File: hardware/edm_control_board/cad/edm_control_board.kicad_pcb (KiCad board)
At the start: 4 copper layers, 240 x 100 mm, 63 parts, among them J401 Conn_02x08_Odd_Even, J402 Conn_01x02, J403 Conn_01x02, J404 Conn_01x02, J405 Conn_01x06, Q201 BSS214NW, Q202 BSS214NW, Q203 BSS214NW, Q204 BSS214NW, SW501 SW_Push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

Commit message: Routing
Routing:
- net /Controller/LCD_DB6: track 75.6 -> 78.1 mm
- net /Controller/LCD_DB5: track 75.3 -> 76.8 mm
- net /Controller/LCD_DB7: track 77.8 -> 79.3 mm
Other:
- board text added: "EDM Control Board 2018-02-18 JS"
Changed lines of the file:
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@@
   (general
     (thickness 1.6)
-    (drawings 34)
-    (tracks 496)
+    (drawings 35)
+    (tracks 500)
     (zones 0)
     (modules 63)
@@
   )
   (setup
-    (last_trace_width 1)
+    (last_trace_width 0.25)
     (user_trace_width 0.25)
     (user_trace_width 0.5)
@@
     )
   )
+  (gr_text "EDM Control Board 2018-02-18 JS" (at 16 -3) (layer B.SilkS)
+    (effects (font (size 1.5 1.5) (thickness 0.3)) (justify right mirror))
+  )
   (gr_text SWDIO (at 129.74 -93.33 270) (layer B.SilkS)
     (effects (font (size 1 1) (thickness 0.2)) (justify left mirror))
@@
   (segment (start 171.25 -65.532055) (end 152.782055 -84) (width 0.25) (layer B.Cu) (net 39))
   (segment (start 171.25 -63.95) (end 171.25 -65.532055) (width 0.25) (layer B.Cu) (net 39))
-  (segment (start 152.6456 -83.500044) (end 107.040044 -83.500044) (width 0.25) (layer B.Cu) (net 40))
-  (segment (start 170.75 -65.395644) (end 152.6456 -83.500044) (width 0.25) (layer B.Cu) (net 40))
-  (segment (start 105.749999 -82.209999) (end 105 -81.46) (width 0.25) (layer B.Cu) (net 40))
+  (segment (start 105.04 -81.5) (end 105 -81.46) (width 0.25) (layer B.Cu) (net 40))
   (segment (start 170.75 -63.95) (end 170.75 -65.395644) (width 0.25) (layer B.Cu) (net 40))
-  (segment (start 107.040044 -83.500044) (end 105.749999 -82.209999) (width 0.25) (layer B.Cu) (net 40))
-  (segment (start 105 -78.92) (end 109.130033 -83.050033) (width 0.25) (layer B.Cu) (net 41))
-  (segment (start 169.25 -64.7) (end 169.25 -63.95) (width 0.25) (layer B.Cu) (net 41))
-  (segment (start 169.25 -66.259233) (end 169.25 -64.7) (width 0.25) (layer B.Cu) (net 41))
+  (segment (start 108.200044 -83.500044) (end 106.2 -81.5) (width 0.25) (layer B.Cu) (net 40))
+  (segment (start 152.6456 -83.500044) (end 108.200044 -83.500044) (width 0.25) (layer B.Cu) (net 40))
+  (segment (start 170.75 -65.395644) (end 152.6456 -83.500044) (width 0.25) (layer B.Cu) (net 40))
+  (segment (start 106.2 -81.5) (end 105.04 -81.5) (width 0.25) (layer B.Cu) (net 40))
+  (segment (start 106.5 -81.109233) (end 108.4408 -83.050033) (width 0.25) (layer B.Cu) (net 41))
+  (segment (start 105 -78.92) (end 106.5 -80.42) (width 0.25) (layer B.Cu) (net 41))
+  (segment (start 106.5 -80.42) (end 106.5 -81.109233) (width 0.25) (layer B.Cu) (net 41))
+  (segment (start 108.4408 -83.050033) (end 152.4592 -83.050033) (width 0.25) (layer B.Cu) (net 41))
   (segment (start 152.4592 -83.050033) (end 169.25 -66.259233) (width 0.25) (layer B.Cu) (net 41))
-  (segment (start 109.130033 -83.050033) (end 152.4592 -83.050033) (width 0.25) (layer B.Cu) (net 41))
-  (segment (start 105 -76.38) (end 111.220022 -82.600022) (width 0.25) (layer B.Cu) (net 42))
+  (segment (start 169.25 -66.259233) (end 169.25 -64.7) (width 0.25) (layer B.Cu) (net 41))
+  (segment (start 169.25 -64.7) (end 169.25 -63.95) (width 0.25) (layer B.Cu) (net 41))
   (segment (start 168.75 -64.7) (end 168.75 -63.95) (width 0.25) (layer B.Cu) (net 42))
-  (segment (start 111.220022 -82.600022) (end 152.2728 -82.600022) (width 0.25) (layer B.Cu) (net 42))
-  (segment (start 152.2728 -82.600022) (end 168.75 -66.122822) (width 0.25) (layer B.Cu) (net 42))
   (segment (start 168.75 -66.122822) (end 168.75 -64.7) (width 0.25) (layer B.Cu) (net 42))
-  (segment (start 105 -73.84) (end 105.749999 -74.589999) (width 0.25) (layer B.Cu) (net 43))
-  (segment (start 105.749999 -74.589999) (end 105.749999 -74.84077) (width 0.25) (layer B.Cu) (net 43))
+  (segment (start 152.2728 -82.600022) (end 168.75 -66.122822) (width 0.25) (layer B.Cu) (net 42))
+  (segment (start 108.6272 -82.600022) (end 152.2728 -82.600022) (width 0.25) (layer B.Cu) (net 42))
+  (segment (start 105 -76.38) (end 106.950011 -78.330011) (width 0.25) (layer B.Cu) (net 42))
+  (segment (start 106.950011 -78.330011) (end 106.950011 -80.922833) (width 0.25) (layer B.Cu) (net 42))
+  (segment (start 106.950011 -80.922833) (end 108.6272 -82.600022) (width 0.25) (layer B.Cu) (net 42))
   (segment (start 168.25 -64.7) (end 168.25 -63.95) (width 0.25) (layer B.Cu) (net 43))
-  (segment (start 152.0864 -82.150011) (end 168.25 -65.986411) (width 0.25) (layer B.Cu) (net 43))
-  (segment (start 113.05924 -82.150011) (end 152.0864 -82.150011) (width 0.25) (layer B.Cu) (net 43))
-  (segment (start 105.749999 -74.84077) (end 113.05924 -82.150011) (width 0.25) (layer B.Cu) (net 43))
   (segment (start 168.25 -65.986411) (end 168.25 -64.7) (width 0.25) (layer B.Cu) (net 43))
-  (segment (start 109.5 -77.95436) (end 113.24564 -81.7) (width 0.25) (layer B.Cu) (net 44))
-  (segment (start 105 -71.3) (end 106.8 -71.3) (width 0.25) (layer B.Cu) (net 44))
-  (segment (start 106.8 -71.3) (end 109.5 -74) (width 0.25) (layer B.Cu) (net 44))
-  (segment (start 109.5 -74) (end 109.5 -77.95436) (width 0.25) (layer B.Cu) (net 44))
-  (segment (start 113.24564 -81.7) (end 151.9 -81.7) (width 0.25) (layer B.Cu) (net 44))
-  (segment (start 151.9 -81.7) (end 167.75 -65.85) (width 0.25) (layer B.Cu) (net 44))
+  (segment (start 152.0864 -82.150011) (end 168.25 -65.986411) (width 0.25) (layer B.Cu) (net 43))
+  (segment (start 108.8136 -82.150011) (end 152.0864 -82.150011) (width 0.25) (layer B.Cu) (net 43))
+  (segment (start 107.449989 -80.7864) (end 108.8136 -82.150011) (width 0.25) (layer B.Cu) (net 43))
+  (segment (start 105 -73.84) (end 107.449989 -76.289989) (width 0.25) (layer B.Cu) (net 43))
+  (segment (start 107.449989 -76.289989) (end 107.449989 -80.7864) (width 0.25) (layer B.Cu) (net 43))
   (segment (start 167.75 -65.85) (end 167.75 -63.95) (width 0.25) (layer B.Cu) (net 44))
+  (segment (start 151.9 -81.7) (end 167.75 -65.85) (width 0.25) (layer B.Cu) (net 44))
+  (segment (start 109 -81.7) (end 151.9 -81.7) (width 0.25) (layer B.Cu) (net 44))
+  (segment (start 107.9 -80.6) (end 109 -81.7) (width 0.25) (layer B.Cu) (net 44))
+  (segment (start 105 -71.3) (end 107.9 -74.2) (width 0.25) (layer B.Cu) (net 44))
+  (segment (start 107.9 -74.2) (end 107.9 -80.6) (width 0.25) (layer B.Cu) (net 44))
   (segment (start 168.25 -52.55) (end 168.25 -47.605) (width 0.25) (layer B.Cu) (net 45))
   (segment (start 168.25 -47.605) (end 168.555 -47.3) (width 0.25) (layer B.Cu) (net 45))

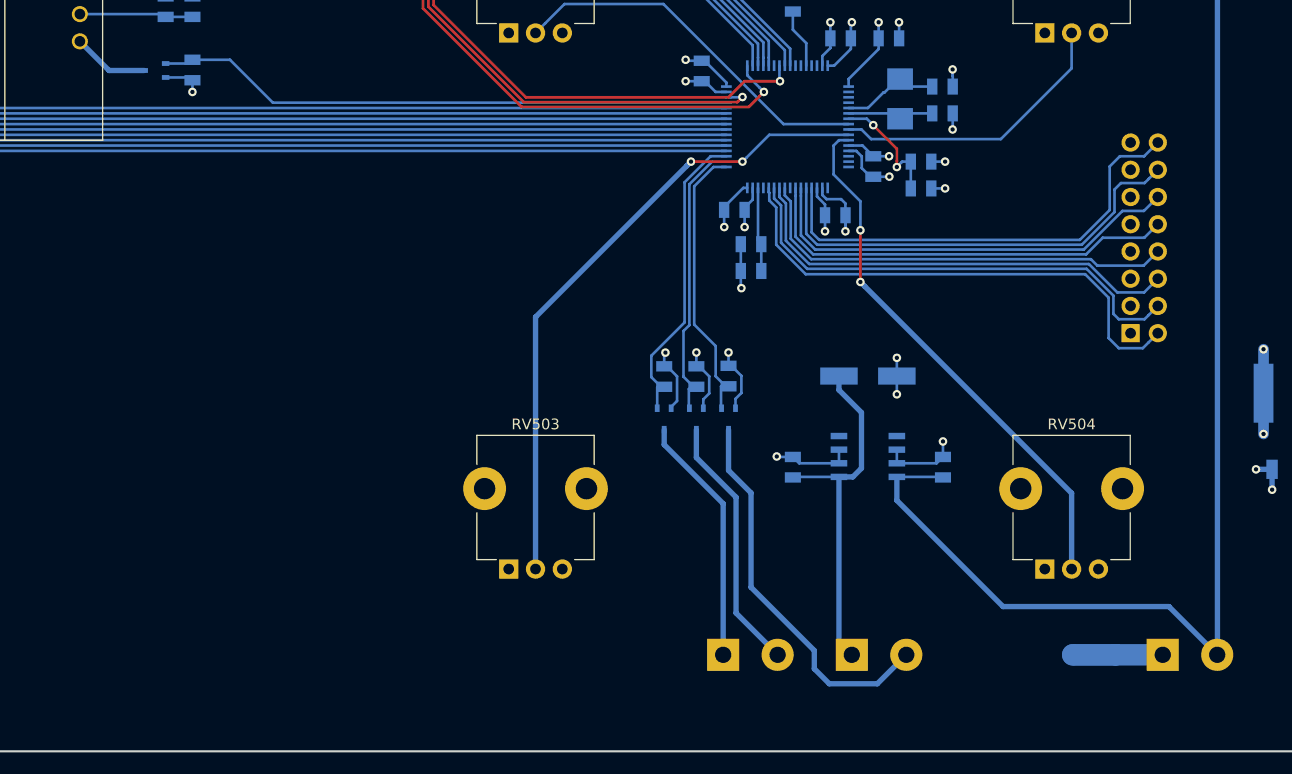
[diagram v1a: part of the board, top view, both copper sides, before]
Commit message: Add water pump to pcb
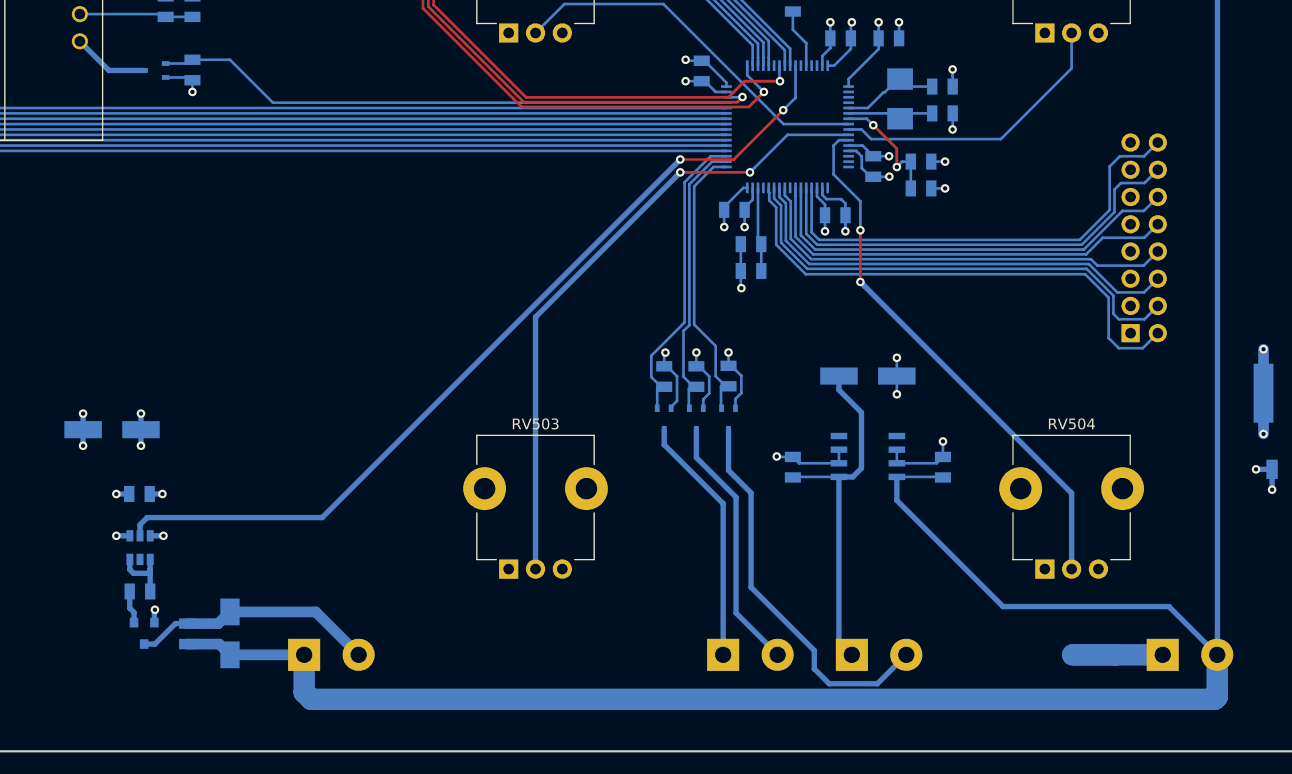
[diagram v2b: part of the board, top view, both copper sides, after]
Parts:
- added C601: 10u, Capacitor_SMD:CP_Elec_6.3x5.3, B.Cu at (108.0, -30.0)
- added C602: 100n, Capacitor_SMD:C_0805_2012Metric, B.Cu at (110.6, -24.0)
- added C603: 1n, Capacitor_SMD:C_0805_2012Metric, B.Cu at (115.0, -11.0)
- added D601: CDBA140-G, Diode_SMD:D_SMA, B.Cu at (119.0, -11.0)
- added J406: Conn_01x02, TerminalBlock:TerminalBlock_bornier-2_P5.08mm, B.Cu at (125.9, -9.00)
- added Q601: DMN3404L-7, Package_TO_SOT_SMD:SOT-23, B.Cu at (111.0, -11.0)
- added R601: 4R99, Resistor_SMD:R_0805_2012Metric, B.Cu at (110.6, -14.9)
- added U601: ZXGD3009E6, Package_TO_SOT_SMD:SOT-23-6, B.Cu at (110.6, -19.0)
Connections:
- U301 pad 58: Net-(U301-Pad58) -> /Controller/Water_Pump_PWM
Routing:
- net +24V: track 139.2 -> 243.4 mm
- net /Controller/Water_Pump_PWM: track 0.00 -> 81.7 mm, vias 0 -> 2
- net /Connectors/Water_Pump_NEG: track 0.00 -> 22.9 mm
- net GND: track 105.8 -> 112.5 mm, vias 29 -> 34
- net Net-(R601-Pad2): track 0.00 -> 6.39 mm
- net +3V3: track 42.8 -> 48.3 mm, vias 12 -> 16
- net Net-(Q601-Pad1): track 0.00 -> 3.07 mm
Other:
- board text added: "PUMP+"
- board text added: "PUMP-"

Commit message: Added copper planes to front and back. Added gerber files.
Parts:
- moved RV201 8.00 mm to (41.0, -85.0)
- moved J405 3.00 mm to (122.1, -88.1)
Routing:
- net /Controller/LCD_V0: track 21.8 -> 14.3 mm
- net +24V: track 243.4 -> 239.0 mm
- net /Controller/POT_4: track 50.3 -> 54.3 mm
- net /Connectors/SWCLK: track 70.5 -> 67.2 mm
- net /Connectors/SWDIO: track 61.3 -> 58.1 mm
- net /Connectors/SWO: track 60.8 -> 58.6 mm
- added copper zone on B.Cu, net /Connectors/Shield
- added copper zone on In1.Cu, net /Connectors/Shield
- added copper zone on In2.Cu, net /Connectors/Shield
- added copper zone on B.Cu, net GND
- added copper zone on F.Cu, net GND

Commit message: Change terminal name from GND to +5V
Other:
- board text added: "+5V"
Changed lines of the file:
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@@
   (page A4)
   (layers
-    (0 F.Cu signal)
+    (0 F.Cu signal hide)
     (1 In1.Cu power hide)
     (2 In2.Cu power hide)
-    (31 B.Cu signal hide)
+    (31 B.Cu signal)
     (32 B.Adhes user)
     (33 F.Adhes user)
@@
     (effects (font (size 1.5 1.5) (thickness 0.3)) (justify left mirror))
   )
-  (gr_text GND (at 177 -14 270) (layer B.SilkS)
+  (gr_text +5V (at 177 -14 270) (layer B.SilkS)
     (effects (font (size 1.5 1.5) (thickness 0.3)) (justify left mirror))
   )
